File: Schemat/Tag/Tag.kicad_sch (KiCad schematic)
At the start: 2 parts, among them U1 SX1276, U2 ESP32-C3

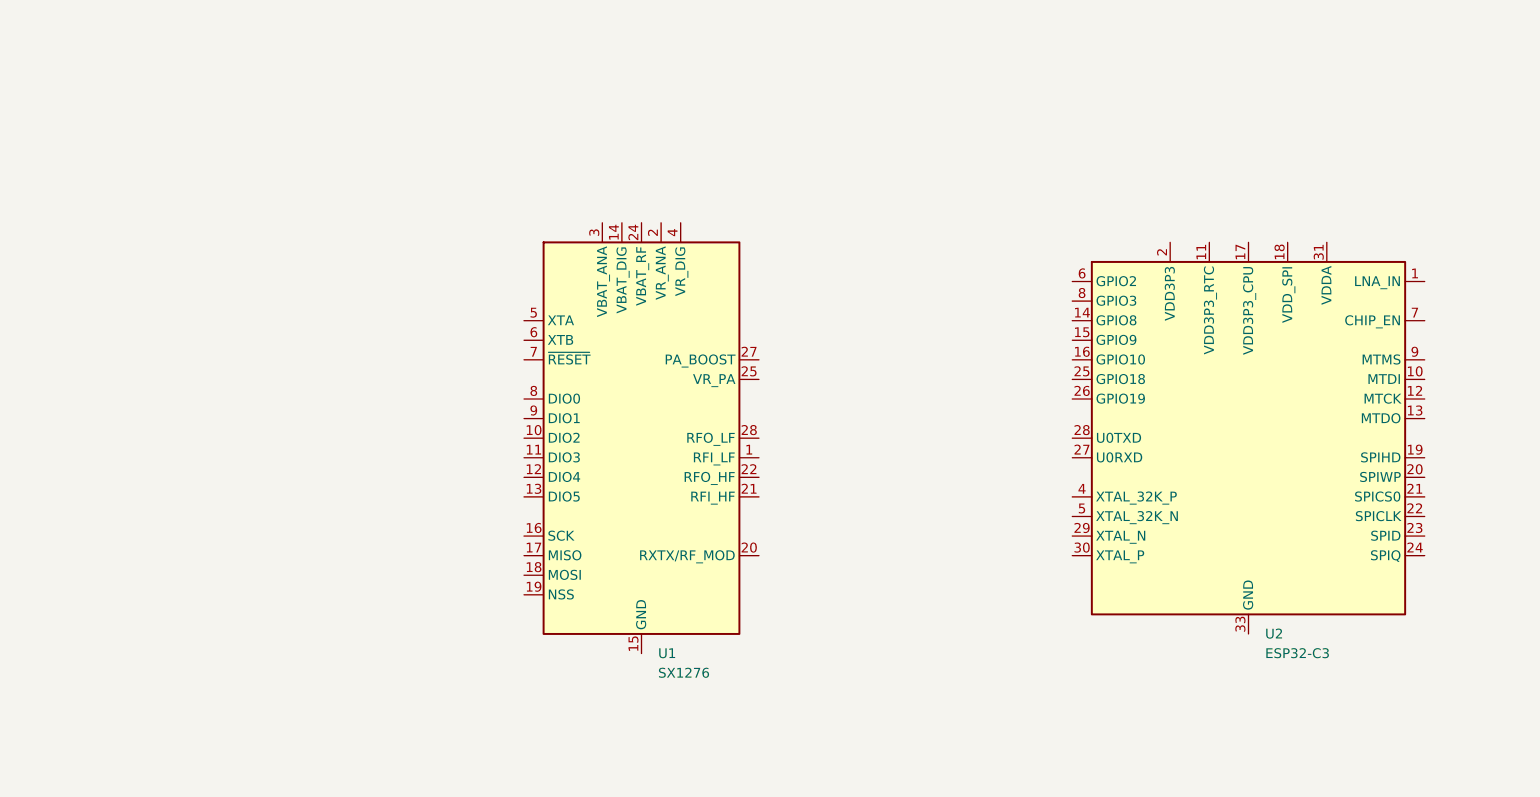
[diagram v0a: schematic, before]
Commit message: Hubert 21.03 - 18:15
Pierwotny zarys schematu, dobór oscylatora, mikrokontrolera i doporowadzenie zasilania do układu LORA SX1276
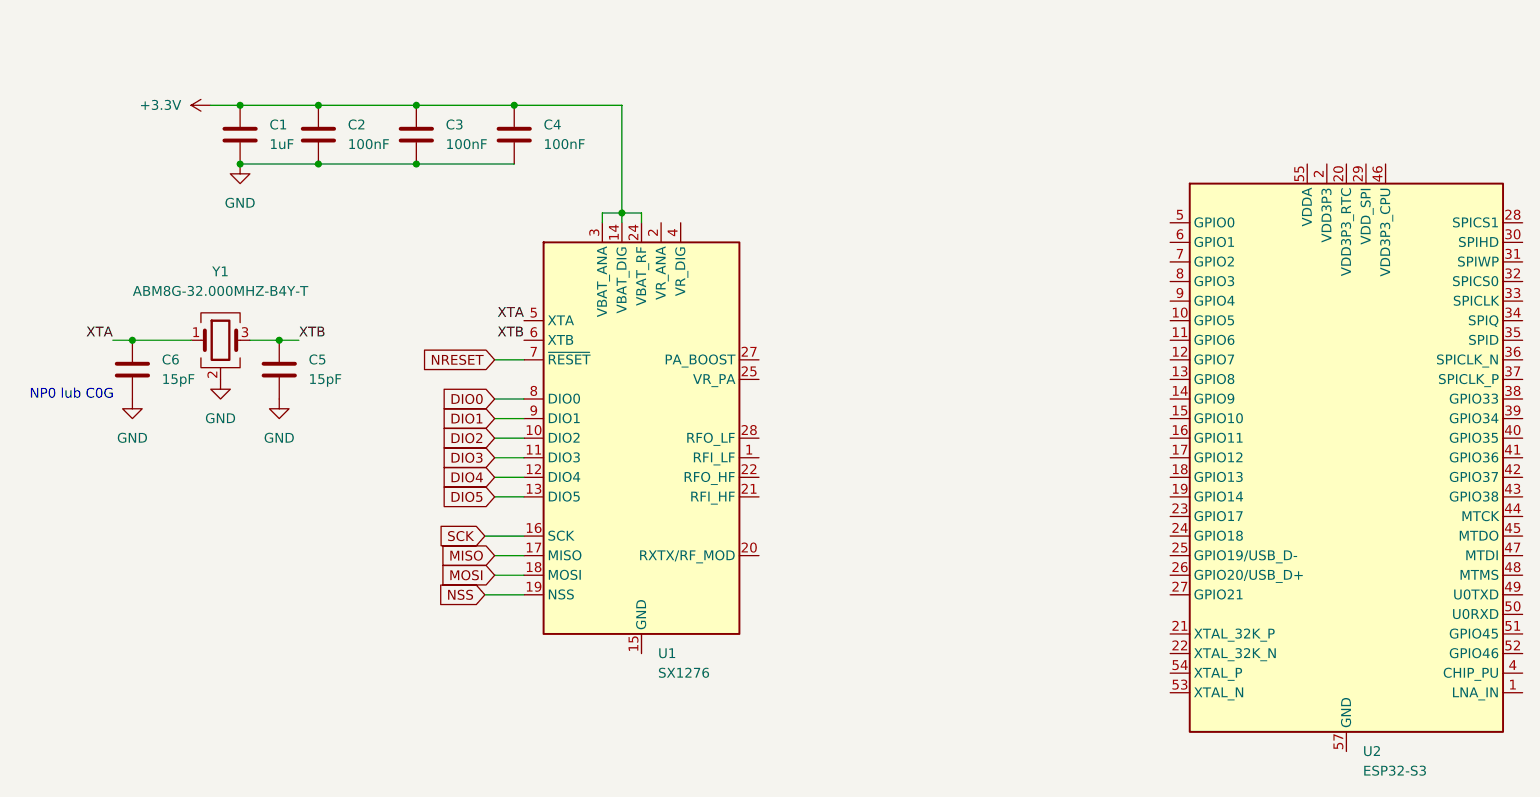
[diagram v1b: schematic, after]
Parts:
- removed U2: ESP32-C3, Package_DFN_QFN:QFN-32-1EP_5x5mm_P0.5mm_EP3.7x3.7mm, symbol MCU_Espressif:ESP32-C3
- added C1: 1uF, symbol Device:C
- added C2, C3, C4: 100nF, symbol Device:C
- added C5, C6: 15pF, symbol Device:C
- added U2: ESP32-S3, Package_DFN_QFN:QFN-56-1EP_7x7mm_P0.4mm_EP4x4mm, symbol MCU_Espressif:ESP32-S3
- added Y1: ABM8G-32.000MHZ-B4Y-T, symbol Device:Crystal_GND24
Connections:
- net DIO2: now reaches U1.10 (DIO2)
- net DIO3: now reaches U1.11 (DIO3)
- net DIO4: now reaches U1.12 (DIO4)
- net DIO5: now reaches U1.13 (DIO5)
- net +3.3V: now reaches U1.14 (VBAT_DIG)
- net +3.3V: now also U1.24 (VBAT_RF), U1.3 (VBAT_ANA), C1.1, C2.1, C3.1, C4.1
- net SCK: now reaches U1.16 (SCK)
- net MISO: now reaches U1.17 (MISO)
- net MOSI: now reaches U1.18 (MOSI)
- net NSS: now reaches U1.19 (NSS)
- net XTA: now reaches U1.5 (XTA)
- net XTA: now also C6.1, Y1.1
- net XTB: now reaches U1.6 (XTB)
- net XTB: now also C5.1, Y1.3
- net NRESET: now reaches U1.7 (~{RESET})
- net DIO0: now reaches U1.8 (DIO0)
- net DIO1: now reaches U1.9 (DIO1)
- new net: U2.2 (VDD3P3), U2.3 (VDD3P3)
- new net: U2.55 (VDDA), U2.56 (VDDA)
- new net GND: C1.2, C2.2, C3.2, C4.2, C5.2, C6.2, Y1.2 (G), Y1.4 (G)
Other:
- note added: "NP0 lub C0G"

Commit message: Hubert 23.03
Zmiany dodanie rezystorów PULL-UP i niewielkie zmiany połączeń pomiędzy modułem LORA, a ESP32
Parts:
- added C7: 100nF, symbol Device:C
- added R1, R2: 10k, symbol Device:R
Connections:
- net +3.3V: now also R1.1, R2.1
- net DIO0: now also U2.19 (GPIO14)
- net DIO1: now also U2.23 (GPIO17)
- net DIO2: now also U2.24 (GPIO18)
- net DIO3: now also U2.25 (GPIO19/USB_D-)
- net DIO4: now also U2.26 (GPIO20/USB_D+)
- net DIO5: now also U2.27 (GPIO21)
- net GND: now also C7.1
- net MISO: now also U2.18 (GPIO13)
- net MOSI: now also U2.16 (GPIO11)
- net NRESET: now also U2.14 (GPIO9), C7.2, R2.2
- net NSS: now also U2.15 (GPIO10), R1.2
- net SCK: now also U2.17 (GPIO12)
- no-connect marks 0 -> 3
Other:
- note added: "PULL-UP"
- note added: "PULL-UP DEBOUNCE"

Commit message: Wesja Beta skończona do weryfikacji
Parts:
- removed C1: 1uF, symbol Device:C
- removed C2, C3, C4, C7: 100nF, symbol Device:C
- removed C5, C6: 15pF, symbol Device:C
- removed R1, R2: 10k, symbol Device:R
- removed U1: SX1276, Package_DFN_QFN:QFN-28-1EP_6x6mm_P0.65mm_EP4.8x4.8mm, symbol RF:SX1276
- removed U2: ESP32-S3, Package_DFN_QFN:QFN-56-1EP_7x7mm_P0.4mm_EP4x4mm, symbol MCU_Espressif:ESP32-S3
- removed Y1: ABM8G-32.000MHZ-B4Y-T, symbol Device:Crystal_GND24
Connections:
- no-connect marks 3 -> 0
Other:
- added sheet ESP32 (ESP32.kicad_sch)
- added sheet Peripherals (Peripherals.kicad_sch)
- added sheet PowerInput (PowerInput.kicad_sch)
- note removed: "NP0 lub C0G"
- note removed: "PULL-UP"
- note removed: "PULL-UP DEBOUNCE"
